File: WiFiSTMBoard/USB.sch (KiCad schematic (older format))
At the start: 3 parts

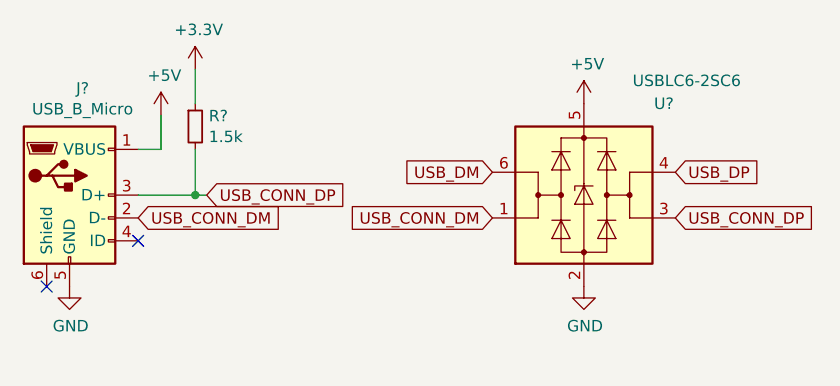
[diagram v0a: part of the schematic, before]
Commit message: finished serial circuit
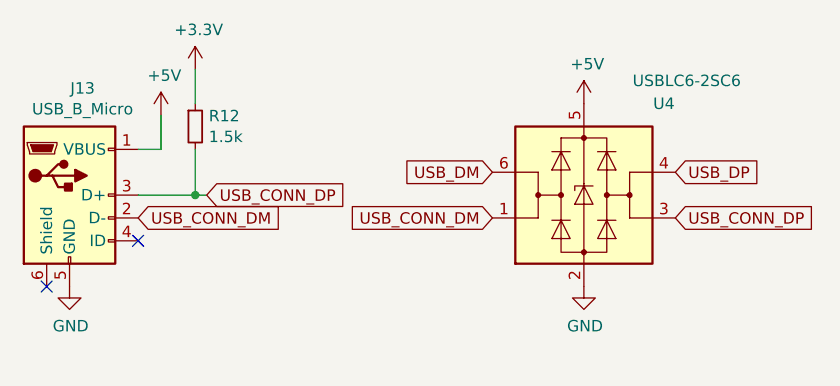
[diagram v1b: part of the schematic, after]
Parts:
- gave numbers to parts that had none: 3
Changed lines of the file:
@@
 $EndDescr
 $Comp
-L Connector:USB_B_Micro J?
+L Connector:USB_B_Micro J13
 U 1 1 61956506
 P 2450 1450
-F 0 "J?" H 2507 1917 50  0000 C CNN
+F 0 "J13" H 2507 1917 50  0000 C CNN
 F 1 "USB_B_Micro" H 2507 1826 50  0000 C CNN
 F 2 "" H 2600 1400 50  0001 C CNN
@@
 NoConn ~ 2350 1850
 $Comp
-L power:GND #PWR?
+L power:GND #PWR0161
 U 1 1 61958F68
 P 2450 1850
-F 0 "#PWR?" H 2450 1600 50  0001 C CNN
+F 0 "#PWR0161" H 2450 1600 50  0001 C CNN
 F 1 "GND" H 2455 1677 50  0000 C CNN
 F 2 "" H 2450 1850 50  0001 C CNN
@@
 $EndComp
 $Comp
-L Power_Protection:USBLC6-2SC6 U?
+L Power_Protection:USBLC6-2SC6 U4
 U 1 1 61959619
 P 4700 1450
-F 0 "U?" H 5050 1850 50  0000 C CNN
+F 0 "U4" H 5050 1850 50  0000 C CNN
 F 1 "USBLC6-2SC6" H 5150 1950 50  0000 C CNN
 F 2 "Package_TO_SOT_SMD:SOT-23-6" H 4700 950 50  0001 C CNN
@@
 $EndComp
 $Comp
-L power:+5V #PWR?
+L power:+5V #PWR0162
 U 1 1 6196211F
 P 2850 1100
-F 0 "#PWR?" H 2850 950 50  0001 C CNN
+F 0 "#PWR0162" H 2850 950 50  0001 C CNN
 F 1 "+5V" H 2865 1273 50  0000 C CNN
 F 2 "" H 2850 1100 50  0001 C CNN
@@
 NoConn ~ 2750 1650
 $Comp
-L power:+5V #PWR?
+L power:+5V #PWR0163
 U 1 1 61967FA4
 P 4700 1050
-F 0 "#PWR?" H 4700 900 50  0001 C CNN
+F 0 "#PWR0163" H 4700 900 50  0001 C CNN
 F 1 "+5V" H 4715 1223 50  0000 C CNN
 F 2 "" H 4700 1050 50  0001 C CNN
@@
 $EndComp
 $Comp
-L power:GND #PWR?
+L power:GND #PWR0164
 U 1 1 619683BB
 P 4700 1850
-F 0 "#PWR?" H 4700 1600 50  0001 C CNN
+F 0 "#PWR0164" H 4700 1600 50  0001 C CNN
 F 1 "GND" H 4705 1677 50  0000 C CNN
 F 2 "" H 4700 1850 50  0001 C CNN
@@
 	2750 1450 3000 1450
 $Comp
-L Device:R_Small R?
+L Device:R_Small R12
 U 1 1 6196B36B
 P 3000 1150
-F 0 "R?" H 3059 1196 50  0000 L CNN
+F 0 "R12" H 3059 1196 50  0000 L CNN
 F 1 "1.5k" H 3059 1105 50  0000 L CNN
 F 2 "" H 3000 1150 50  0001 C CNN
@@
 	3000 1450 3050 1450
 $Comp
-L power:+3.3V #PWR?
+L power:+3.3V #PWR0165
 U 1 1 6196B8A4
 P 3000 900
-F 0 "#PWR?" H 3000 750 50  0001 C CNN
+F 0 "#PWR0165" H 3000 750 50  0001 C CNN
 F 1 "+3.3V" H 3015 1073 50  0000 C CNN
 F 2 "" H 3000 900 50  0001 C CNN

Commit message: starting PCB layout
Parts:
- J15: renamed from J13; footprint (none) -> Connector_USB:USB_Micro-B_Amphenol_10118194_Horizontal
- R13: renamed from R12; footprint (none) -> Resistor_SMD:R_0805_2012Metric
- renumbered U4 to U3
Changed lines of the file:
@@
 $Descr User 8268 4016
 encoding utf-8
-Sheet 6 6
+Sheet 5 5
 Title ""
 Date ""
@@
 $EndDescr
 $Comp
-L Connector:USB_B_Micro J13
+L Connector:USB_B_Micro J15
 U 1 1 61956506
 P 2450 1450
-F 0 "J13" H 2507 1917 50  0000 C CNN
+F 0 "J15" H 2507 1917 50  0000 C CNN
 F 1 "USB_B_Micro" H 2507 1826 50  0000 C CNN
-F 2 "" H 2600 1400 50  0001 C CNN
+F 2 "Connector_USB:USB_Micro-B_Amphenol_10118194_Horizontal" H 2600 1400 50  0001 C CNN
 F 3 "~" H 2600 1400 50  0001 C CNN
 	1    2450 1450
@@
 NoConn ~ 2350 1850
 $Comp
-L power:GND #PWR0161
+L power:GND #PWR061
 U 1 1 61958F68
 P 2450 1850
-F 0 "#PWR0161" H 2450 1600 50  0001 C CNN
+F 0 "#PWR061" H 2450 1600 50  0001 C CNN
 F 1 "GND" H 2455 1677 50  0000 C CNN
 F 2 "" H 2450 1850 50  0001 C CNN
@@
 $EndComp
 $Comp
-L Power_Protection:USBLC6-2SC6 U4
+L Power_Protection:USBLC6-2SC6 U3
 U 1 1 61959619
 P 4700 1450
-F 0 "U4" H 5050 1850 50  0000 C CNN
+F 0 "U3" H 5050 1850 50  0000 C CNN
 F 1 "USBLC6-2SC6" H 5150 1950 50  0000 C CNN
 F 2 "Package_TO_SOT_SMD:SOT-23-6" H 4700 950 50  0001 C CNN
@@
 $EndComp
 $Comp
-L power:+5V #PWR0162
+L power:+5V #PWR060
 U 1 1 6196211F
 P 2850 1100
-F 0 "#PWR0162" H 2850 950 50  0001 C CNN
+F 0 "#PWR060" H 2850 950 50  0001 C CNN
 F 1 "+5V" H 2865 1273 50  0000 C CNN
 F 2 "" H 2850 1100 50  0001 C CNN
@@
 NoConn ~ 2750 1650
 $Comp
-L power:+5V #PWR0163
+L power:+5V #PWR059
 U 1 1 61967FA4
 P 4700 1050
-F 0 "#PWR0163" H 4700 900 50  0001 C CNN
+F 0 "#PWR059" H 4700 900 50  0001 C CNN
 F 1 "+5V" H 4715 1223 50  0000 C CNN
 F 2 "" H 4700 1050 50  0001 C CNN
@@
 $EndComp
 $Comp
-L power:GND #PWR0164
+L power:GND #PWR062
 U 1 1 619683BB
 P 4700 1850
-F 0 "#PWR0164" H 4700 1600 50  0001 C CNN
+F 0 "#PWR062" H 4700 1600 50  0001 C CNN
 F 1 "GND" H 4705 1677 50  0000 C CNN
 F 2 "" H 4700 1850 50  0001 C CNN
@@
 	2750 1450 3000 1450
 $Comp
-L Device:R_Small R12
+L Device:R_Small R13
 U 1 1 6196B36B
 P 3000 1150
-F 0 "R12" H 3059 1196 50  0000 L CNN
+F 0 "R13" H 3059 1196 50  0000 L CNN
 F 1 "1.5k" H 3059 1105 50  0000 L CNN
-F 2 "" H 3000 1150 50  0001 C CNN
+F 2 "Resistor_SMD:R_0805_2012Metric" H 3000 1150 50  0001 C CNN
 F 3 "~" H 3000 1150 50  0001 C CNN
 	1    3000 1150
@@
 	3000 1450 3050 1450
 $Comp
-L power:+3.3V #PWR0165
+L power:+3.3V #PWR058
 U 1 1 6196B8A4
 P 3000 900
-F 0 "#PWR0165" H 3000 750 50  0001 C CNN
+F 0 "#PWR058" H 3000 750 50  0001 C CNN
 F 1 "+3.3V" H 3015 1073 50  0000 C CNN
 F 2 "" H 3000 900 50  0001 C CNN
